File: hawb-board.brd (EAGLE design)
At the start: 100 x 74.9 mm, 85 parts, among them IC1 3.3V SR05S3V3, IC2 5V SR05S05, IC3 OPAMP-DUALU, IC4 OPAMP-DUALU, M2 HX1, Q1 MOSFET-NCHANNELFDD8580, Q2 MOSFET-NCHANNELFDD8580, Q3 N-FET, Q4 N-FET, Q5 N-FET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

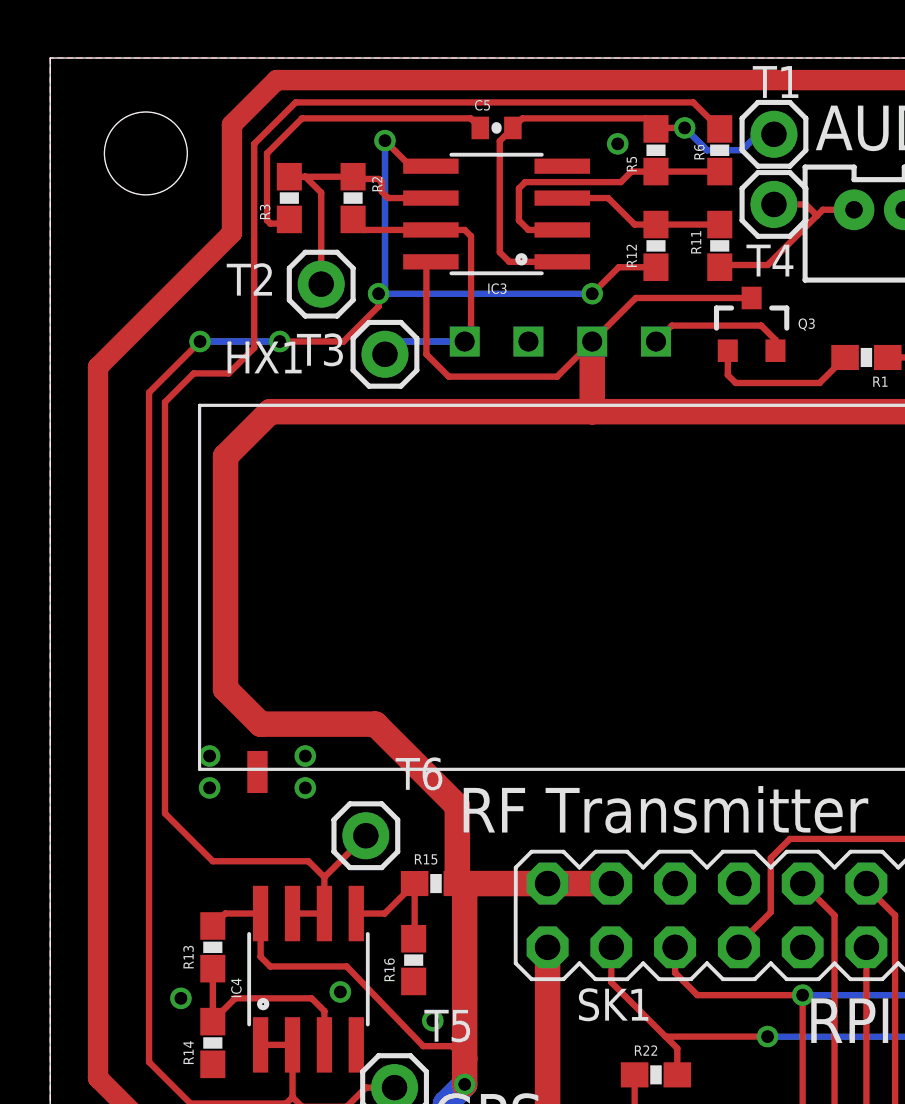
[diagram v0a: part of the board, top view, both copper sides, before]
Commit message: Added some decoupling caps, bom
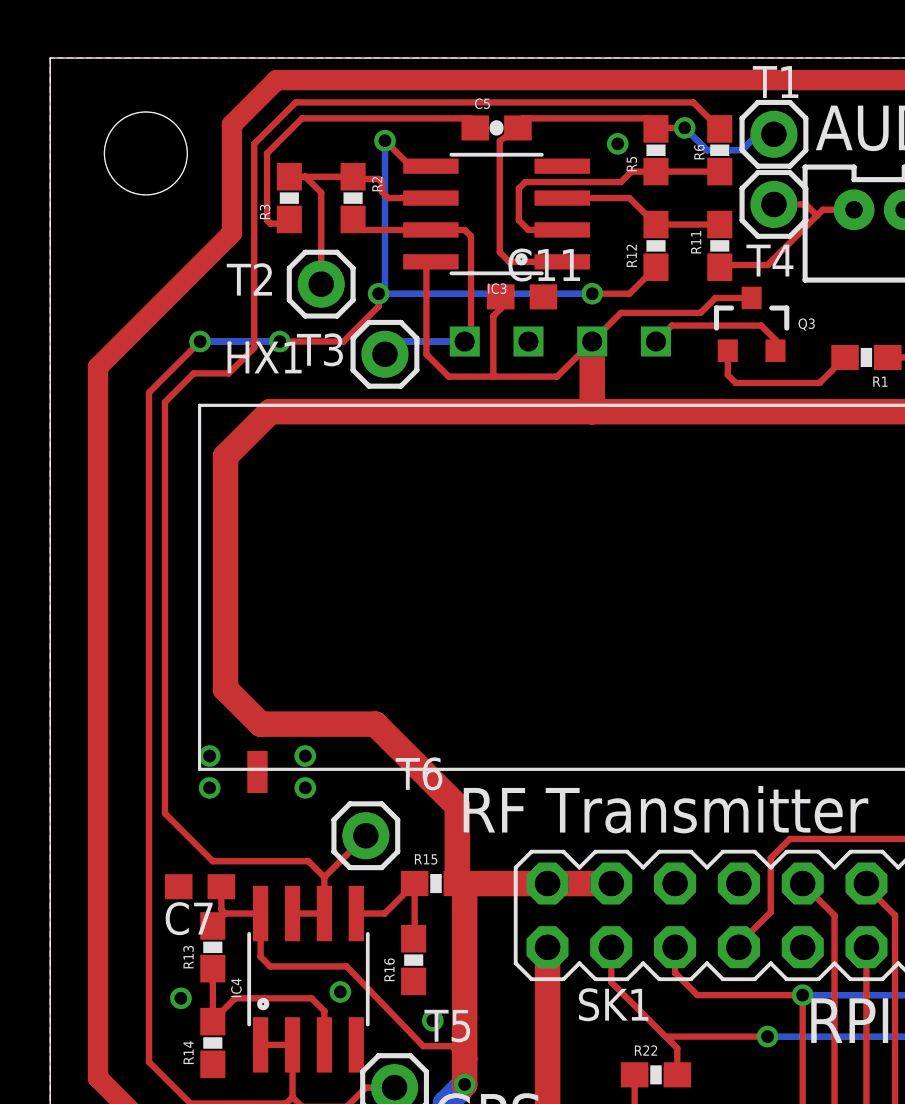
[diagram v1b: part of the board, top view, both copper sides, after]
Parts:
- added C11, C7: 0.1uF, rcl:C0603
- C5: device sparkfun:0402-CAP -> SparkFun-Capacitors:0603-CAP
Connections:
- net 5V: now also C11.1, C7.1
- net GND: now also C11.2, C7.2
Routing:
- net 5V: track 274.6 -> 279.0 mm
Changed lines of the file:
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@@
 <layer number="23" name="tOrigins" color="15" fill="1" visible="yes" active="yes"/>
 <layer number="24" name="bOrigins" color="15" fill="1" visible="yes" active="yes"/>
-<layer number="25" name="tNames" color="7" fill="1" visible="yes" active="yes"/>
+<layer number="25" name="tNames" color="7" fill="1" visible="no" active="yes"/>
 <layer number="26" name="bNames" color="7" fill="1" visible="no" active="yes"/>
 <layer number="27" name="tValues" color="7" fill="1" visible="no" active="yes"/>
@@
 <layer number="146" name="p_Milling" color="3" fill="9" visible="no" active="yes"/>
 <layer number="147" name="COVER" color="14" fill="1" visible="no" active="yes"/>
-<layer number="150" name="Notes" color="7" fill="1" visible="yes" active="yes"/>
+<layer number="150" name="Notes" color="7" fill="1" visible="no" active="yes"/>
 <layer number="151" name="HeatSink" color="7" fill="1" visible="no" active="yes"/>
 <layer number="152" name="_bDocu" color="7" fill="1" visible="no" active="yes"/>
-<layer number="153" name="FabDoc1" color="7" fill="1" visible="yes" active="yes"/>
-<layer number="154" name="FabDoc2" color="7" fill="1" visible="yes" active="yes"/>
-<layer number="155" name="FabDoc3" color="7" fill="1" visible="yes" active="yes"/>
+<layer number="153" name="FabDoc1" color="7" fill="1" visible="no" active="yes"/>
+<layer number="154" name="FabDoc2" color="7" fill="1" visible="no" active="yes"/>
+<layer number="155" name="FabDoc3" color="7" fill="1" visible="no" active="yes"/>
 <layer number="190" name="Comments" color="12" fill="1" visible="no" active="yes"/>
 <layer number="199" name="Contour" color="7" fill="1" visible="no" active="yes"/>
@@
 </element>
 <element name="R12" library="sparkfun" package="0603-RES" value="100k" x="24.13" y="67.31" rot="R90"/>
-<element name="C5" library="sparkfun" package="0402-CAP" value="1nF" x="17.78" y="72.009"/>
+<element name="C5" library="SparkFun-Capacitors" package="0603-CAP" value="1nF" x="17.78" y="72.009"/>
 <element name="IC4" library="sparkfun" package="SO08" value="OPAMP-DUALU" x="10.287" y="38.1" smashed="yes">
 <attribute name="VALUE" x="9.017" y="37.465" size="0.4064" layer="27"/>
@@
 <attribute name="VALUE" x="88.392" y="45.593" size="1.27" layer="27"/>
 </element>
+<element name="C7" library="rcl" package="C0603" value="0.1uF" x="5.969" y="41.783" rot="R180"/>
+<element name="C11" library="rcl" package="C0603" value="0.1uF" x="18.796" y="65.278"/>
 </elements>
 <signals>
@@
 <via x="33.401" y="26.67" extent="1-16" drill="0.508"/>
 <via x="11.557" y="37.592" extent="1-16" drill="0.508"/>
+<contactref element="C7" pad="2"/>
+<contactref element="C11" pad="2"/>
 </signal>
 <signal name="5V">
@@
 <wire x1="8.763" y1="38.608" x2="11.811" y2="38.608" width="0.254" layer="1"/>
 <wire x1="11.811" y1="38.608" x2="14.859" y2="35.433" width="0.254" layer="1"/>
-<wire x1="27.94" y1="65.235" x2="23.325" y2="65.235" width="0.254" layer="1"/>
-<wire x1="23.325" y1="65.235" x2="21.59" y2="63.5" width="0.254" layer="1"/>
 <wire x1="14.859" y1="35.433" x2="16.002" y2="35.433" width="0.254" layer="1"/>
 <wire x1="16.256" y1="41.871" x2="16.217" y2="41.91" width="0.254" layer="1"/>
@@
 <wire x1="8.763" y1="60.706" x2="21.59" y2="60.706" width="1.016" layer="1"/>
 <wire x1="21.59" y1="63.5" x2="20.193" y2="62.103" width="0.254" layer="1"/>
-<wire x1="20.193" y1="62.103" x2="15.875" y2="62.103" width="0.254" layer="1"/>
+<wire x1="20.193" y1="62.103" x2="17.653" y2="62.103" width="0.254" layer="1"/>
+<wire x1="17.653" y1="62.103" x2="15.875" y2="62.103" width="0.254" layer="1"/>
 <wire x1="15.875" y1="62.103" x2="14.986" y2="62.992" width="0.254" layer="1"/>
 <wire x1="14.986" y1="62.992" x2="14.986" y2="66.4972" width="0.254" layer="1"/>
@@
 <wire x1="45.847" y1="13.081" x2="46.355" y2="12.573" width="0.254" layer="1"/>
 <wire x1="46.355" y1="12.573" x2="49.53" y2="12.573" width="0.254" layer="1"/>
+<contactref element="C7" pad="1"/>
+<wire x1="6.819" y1="41.783" x2="6.819" y2="40.8704" width="0.254" layer="1"/>
+<wire x1="6.819" y1="40.8704" x2="6.9732" y2="40.7162" width="0.254" layer="1"/>
+<contactref element="C11" pad="1"/>
+<wire x1="27.94" y1="65.235" x2="26.5" y2="65.235" width="0.254" layer="1"/>
+<wire x1="26.5" y1="65.235" x2="25.908" y2="64.643" width="0.254" layer="1"/>
+<wire x1="25.908" y1="64.643" x2="22.733" y2="64.643" width="0.254" layer="1"/>
+<wire x1="22.733" y1="64.643" x2="21.59" y2="63.5" width="0.254" layer="1"/>
+<wire x1="17.946" y1="65.278" x2="17.946" y2="64.809" width="0.254" layer="1"/>
+<wire x1="17.946" y1="64.809" x2="17.653" y2="64.516" width="0.254" layer="1"/>
+<wire x1="17.653" y1="64.516" x2="17.653" y2="62.103" width="0.254" layer="1"/>
 </signal>
 <signal name="VCC">
@@
 <contactref element="R12" pad="2"/>
 <contactref element="IC3" pad="3"/>
-<wire x1="24.13" y1="68.16" x2="23.28" y2="68.16" width="0.254" layer="1"/>
-<wire x1="23.28" y1="68.16" x2="22.225" y2="69.215" width="0.254" layer="1"/>
-<wire x1="22.225" y1="69.215" x2="20.3962" y2="69.215" width="0.254" layer="1"/>
 <wire x1="26.67" y1="68.16" x2="24.13" y2="68.16" width="0.254" layer="1"/>
+<wire x1="20.3962" y1="69.215" x2="23.075" y2="69.215" width="0.254" layer="1"/>
+<wire x1="23.075" y1="69.215" x2="24.13" y2="68.16" width="0.254" layer="1"/>
 </signal>
 <signal name="N$16">
@@
 <wire x1="18.288" y1="66.675" x2="17.907" y2="67.056" width="0.254" layer="1"/>
 <wire x1="17.907" y1="67.056" x2="17.907" y2="71.486" width="0.254" layer="1"/>
-<wire x1="17.907" y1="71.486" x2="18.43" y2="72.009" width="0.254" layer="1"/>
+<wire x1="17.907" y1="71.486" x2="18.63" y2="72.009" width="0.254" layer="1"/>
 <wire x1="23.71" y1="72.39" x2="18.811" y2="72.39" width="0.254" layer="1"/>
-<wire x1="18.811" y1="72.39" x2="18.43" y2="72.009" width="0.254" layer="1"/>
+<wire x1="18.811" y1="72.39" x2="18.63" y2="72.009" width="0.254" layer="1"/>
 <contactref element="T1" pad="1"/>
 <wire x1="28.829" y1="71.755" x2="28.194" y2="71.755" width="0.254" layer="16"/>
@@
 <via x="9.144" y="63.5" extent="1-16" drill="0.508"/>
 <wire x1="9.144" y1="63.5" x2="5.969" y2="63.5" width="0.254" layer="16"/>
-<wire x1="24.13" y1="66.46" x2="22.645" y2="66.46" width="0.254" layer="1"/>
-<wire x1="22.645" y1="66.46" x2="21.59" y2="65.405" width="0.254" layer="1"/>
 <via x="21.59" y="65.405" extent="1-16" drill="0.508"/>
 <wire x1="21.59" y1="65.405" x2="13.081" y2="65.405" width="0.254" layer="16"/>
@@
 <wire x1="11.811" y1="33.02" x2="10.033" y2="33.02" width="0.254" layer="1"/>
 <wire x1="10.033" y1="33.02" x2="9.652" y2="33.401" width="0.254" layer="1"/>
+<wire x1="21.59" y1="65.405" x2="23.075" y2="65.405" width="0.254" layer="1"/>
+<wire x1="23.075" y1="65.405" x2="24.13" y2="66.46" width="0.254" layer="1"/>
 </signal>
 <signal name="0.5V">
@@
 <wire x1="8.636" y1="70.993" x2="10.033" y2="72.39" width="0.254" layer="1"/>
 <wire x1="10.033" y1="72.39" x2="16.749" y2="72.39" width="0.254" layer="1"/>
-<wire x1="16.749" y1="72.39" x2="17.13" y2="72.009" width="0.254" layer="1"/>
+<wire x1="16.749" y1="72.39" x2="16.93" y2="72.009" width="0.254" layer="1"/>
 </signal>
 <signal name="N$18">

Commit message: Updated board, BOM
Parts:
- moved C4 0.38 mm to (68.2, 41.8)
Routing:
- net 5V: track 279.0 -> 268.4 mm
- net 3.3V: track 321.7 -> 315.6 mm
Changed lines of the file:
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@@
 <element name="C2" library="sparkfun" package="0402-CAP" value="0.1uF" x="68.58" y="38.735" rot="R180"/>
 <element name="C3" library="sparkfun" package="0402-CAP" value="2.2nF" x="76.835" y="39.243" rot="R270"/>
-<element name="C4" library="sparkfun" package="0402-CAP" value="10nF" x="68.58" y="41.783" rot="R180"/>
+<element name="C4" library="sparkfun" package="0402-CAP" value="10nF" x="68.199" y="41.783" rot="R180"/>
 <element name="U1" library="Testing" package="QFN-24-4MM2" value="MPU-6050-1" x="73.025" y="40.64" rot="R270"/>
 <element name="IC3" library="sparkfun" package="SO08" value="OPAMP-DUALU" x="17.78" y="68.58" smashed="yes" rot="R90">
@@
 <wire x1="19.812" y1="41.91" x2="22.352" y2="41.91" width="1.016" layer="1"/>
 <wire x1="19.812" y1="41.91" x2="16.217" y2="41.91" width="1.016" layer="1"/>
-<wire x1="47.244" y1="19.304" x2="45.847" y2="17.907" width="0.254" layer="1"/>
-<wire x1="45.847" y1="17.907" x2="45.847" y2="13.081" width="0.254" layer="1"/>
-<wire x1="45.847" y1="13.081" x2="46.355" y2="12.573" width="0.254" layer="1"/>
-<wire x1="46.355" y1="12.573" x2="49.53" y2="12.573" width="0.254" layer="1"/>
 <contactref element="C7" pad="1"/>
 <wire x1="6.819" y1="41.783" x2="6.819" y2="40.8704" width="0.254" layer="1"/>
@@
 <contactref element="C4" pad="1"/>
 <wire x1="70.9034" y1="41.4021" x2="69.3571" y2="41.4021" width="0.254" layer="1"/>
-<wire x1="69.3571" y1="41.4021" x2="69.23" y2="41.783" width="0.254" layer="1"/>
+<wire x1="69.3571" y1="41.4021" x2="68.849" y2="41.783" width="0.254" layer="1"/>
 </signal>
 <signal name="N$11">
@@
 <wire x1="64.897" y1="43.942" x2="62.865" y2="41.91" width="0.254" layer="1"/>
 <wire x1="60.96" y1="71.882" x2="60.92825" y2="71.91375" width="1.016" layer="1"/>
-<wire x1="66.587" y1="16.93" x2="62.23" y2="12.573" width="0.254" layer="1"/>
 </signal>
 <signal name="N$27">
